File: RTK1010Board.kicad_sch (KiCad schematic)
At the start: 68 parts, among them J1 SMA, J2 IPEX, J3 USB_OTG, J4 BNO055, U1 RTK-1010, U2 MCP1700-3002E_SOT23, U3 MCP1700-3002E_SOT23, U4 ESP32-S2-WROVER

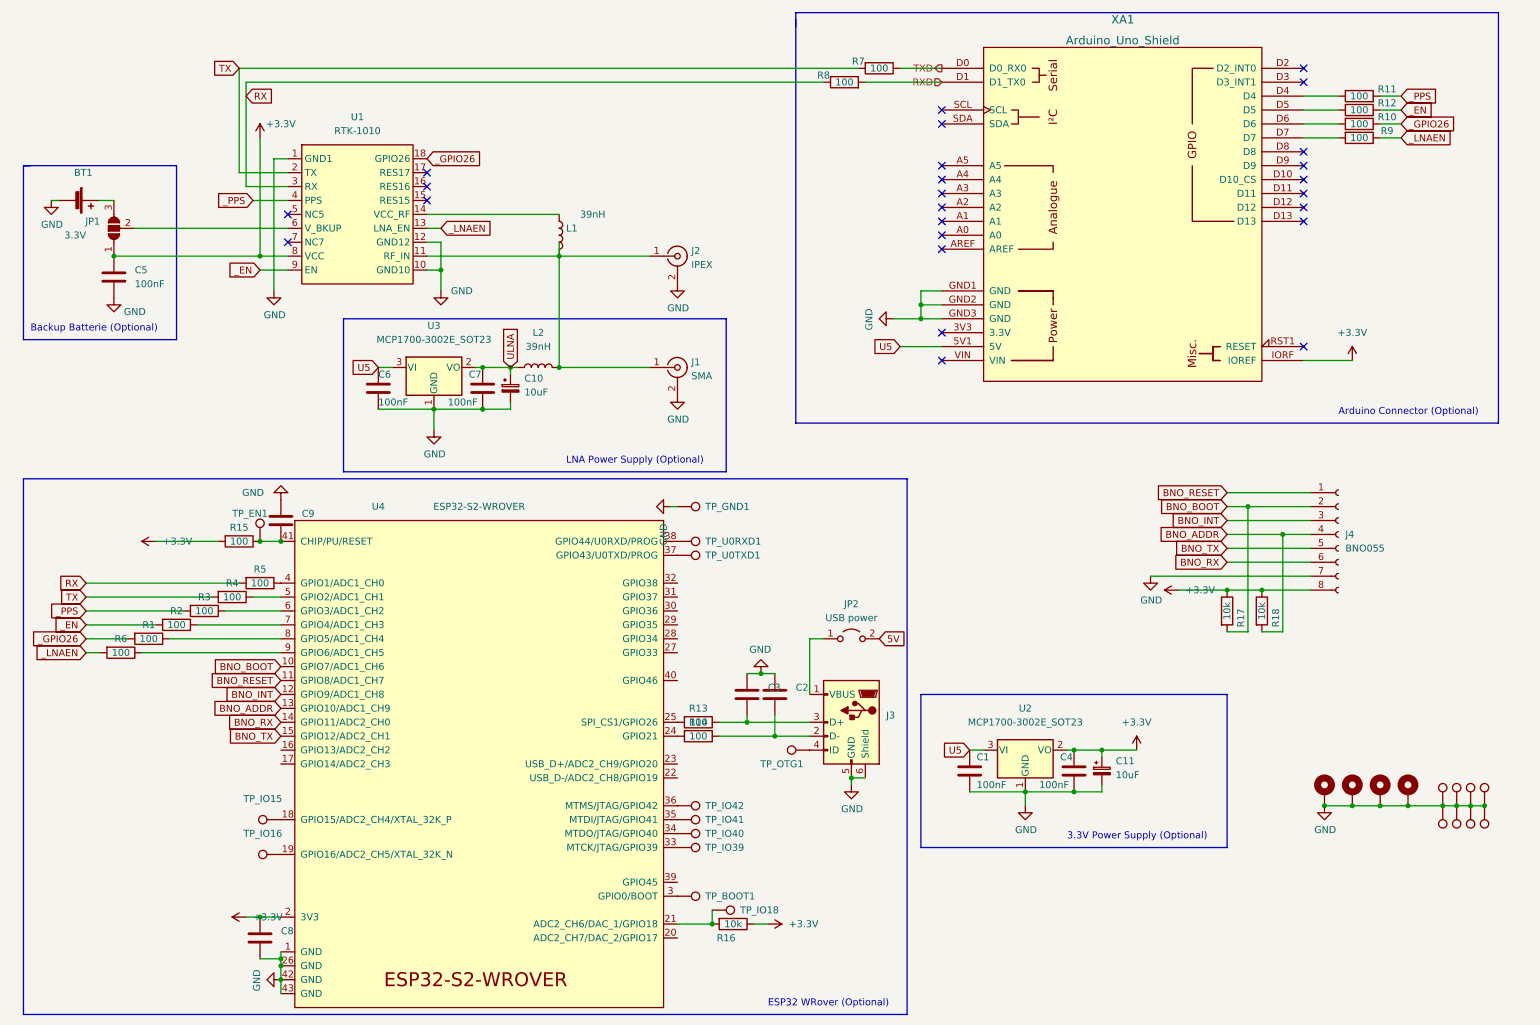
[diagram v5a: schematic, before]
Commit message: UART LoopIn option added USB connected to USB pins
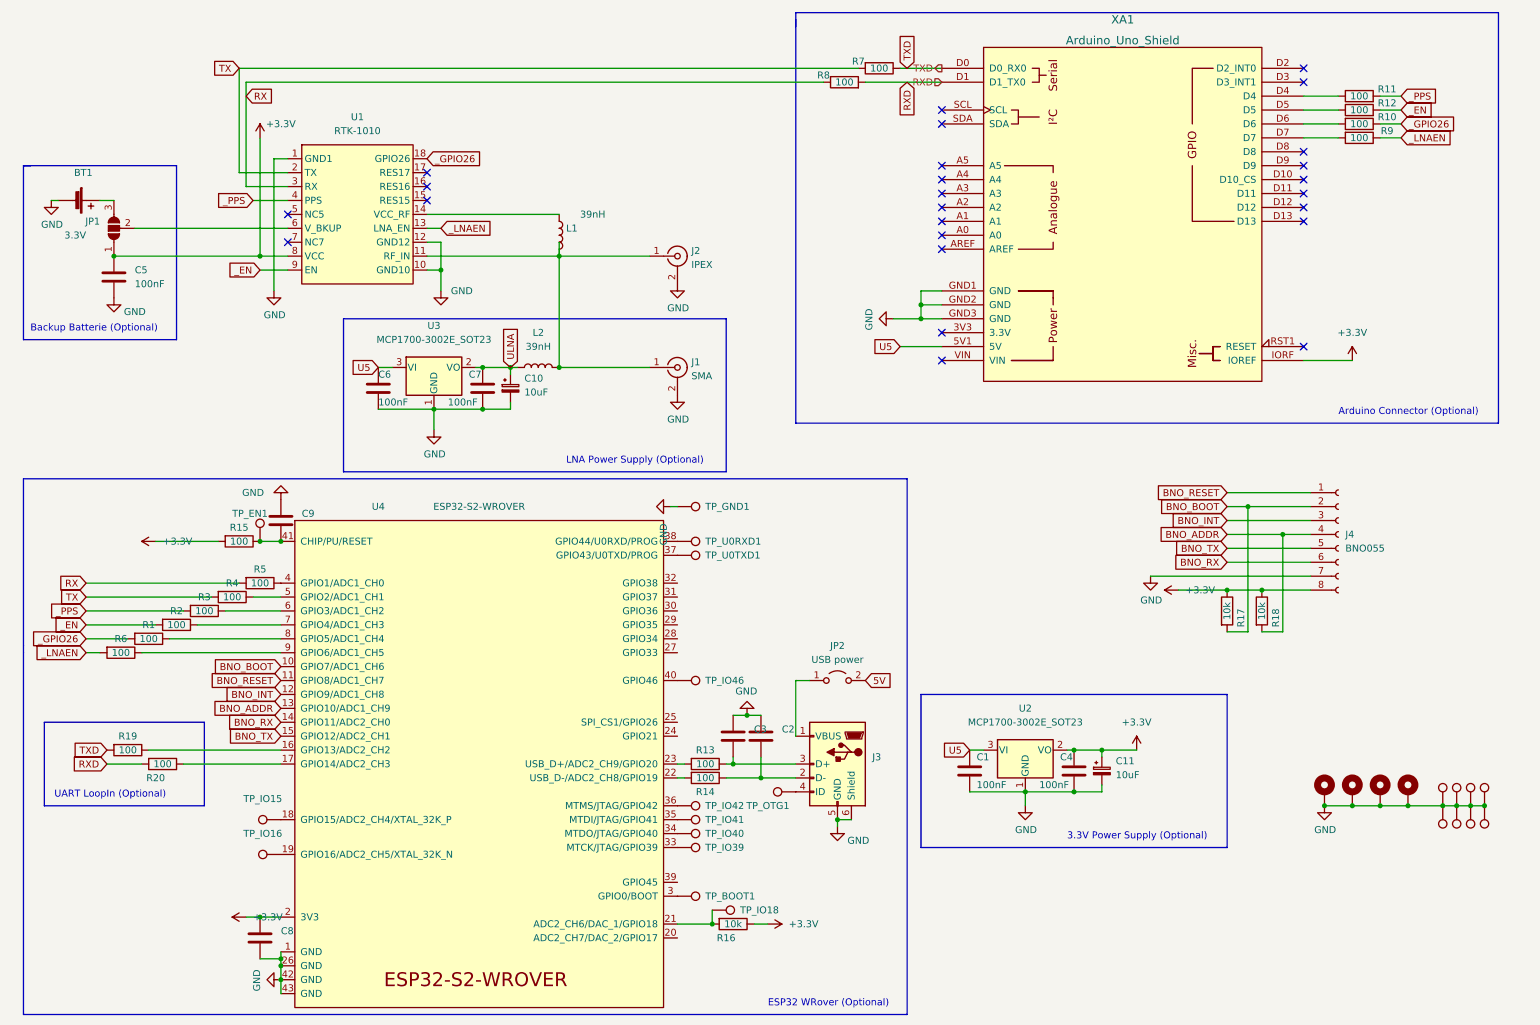
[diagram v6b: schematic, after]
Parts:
- added R19, R20: 100, Resistor_SMD:R_0805_2012Metric_Pad1.20x1.40mm_HandSolder, symbol Device:R
- added TP_IO46: TestPoint, TestPoint:TestPoint_Pad_D2.0mm, symbol Connector:TestPoint
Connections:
- net RXD: now also R20.2
- net TXD: now also R19.2
- net at U4.16 (GPIO13/ADC2_CH2): now also R19.1
- net at U4.17 (GPIO14/ADC2_CH3): now also R20.1
- net at U4.22 (USB_D-/ADC2_CH8/GPIO19): now also R14.2
- net at U4.23 (USB_D+/ADC2_CH9/GPIO20): now also R13.2
- net at U4.24 (GPIO21): no longer R14.2
- net at U4.25 (SPI_CS1/GPIO26): no longer R13.2
- net at U4.40 (GPIO46): now also TP_IO46.1
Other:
- note added: "UART LoopIn (Optional)"
- moved on the sheet: C2, C3, J3, JP2, R13, R14, TP_OTG1
